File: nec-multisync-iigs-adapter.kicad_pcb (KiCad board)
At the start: 2 copper layers, 39.4 x 33 mm, 2 parts, among them J1 DA15_Plug

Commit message: V1 to Fab
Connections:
- J1 pad 1: GND -> /Red_GND
- J1 pad 13: GND -> /Blue_GND
- J1 pad 6: GND -> /Green_GND
- J2 pad 11: unconnected-(J2-Pad11) -> GND
- J2 pad 4: unconnected-(J2-Pad4) -> GND
- J2 pad 6: GND -> /Red_GND
- J2 pad 7: GND -> /Green_GND
- J2 pad 8: GND -> /Blue_GND
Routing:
- net /Blue_GND: track 0.00 -> 26.3 mm, vias 0 -> 2
- net /Green_GND: track 0.00 -> 24.0 mm, vias 0 -> 2
- net /Red_GND: track 0.00 -> 16.2 mm, vias 0 -> 1
- net /CSync: track 35.0 -> 29.4 mm, vias 2 -> 3
- net /Blue: track 29.0 -> 28.8 mm, vias 2 -> 3

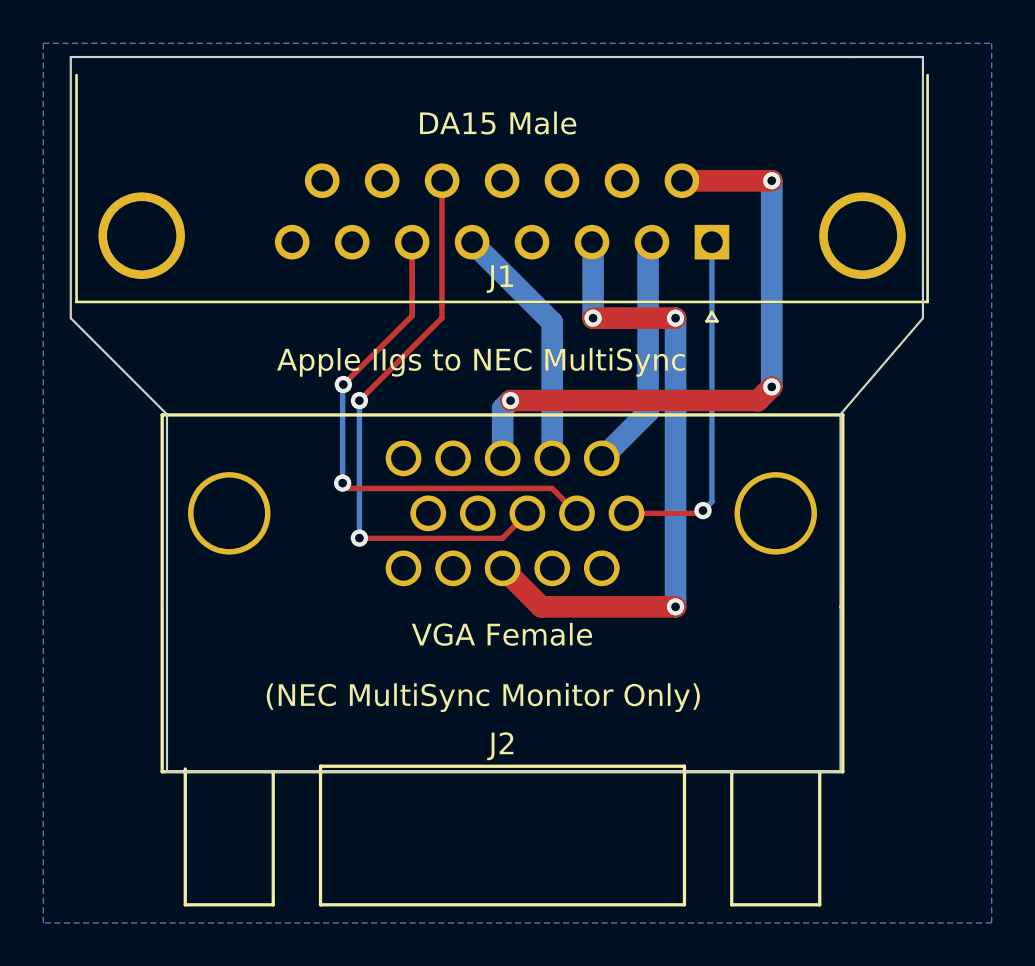
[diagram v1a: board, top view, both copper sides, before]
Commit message: Round-tracks plugin
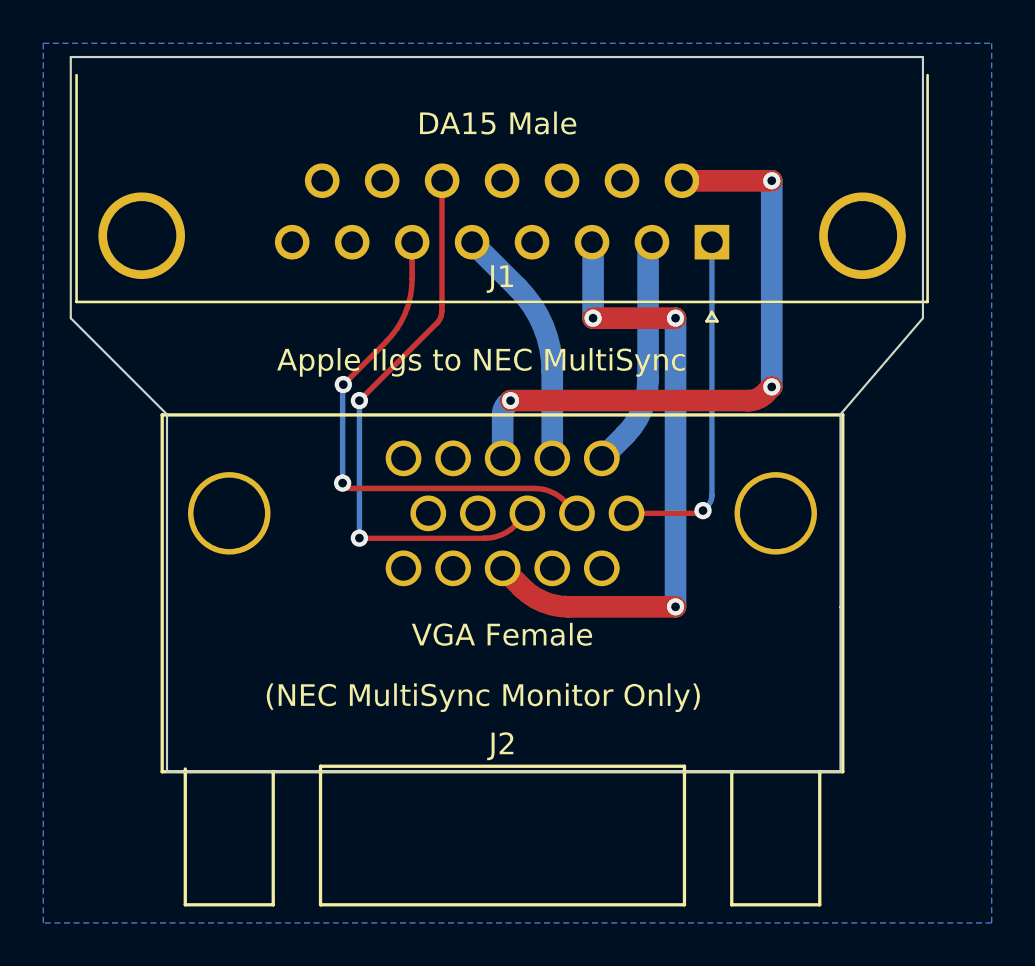
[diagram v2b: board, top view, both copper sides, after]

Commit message: Tie shields together; MultiSync now works
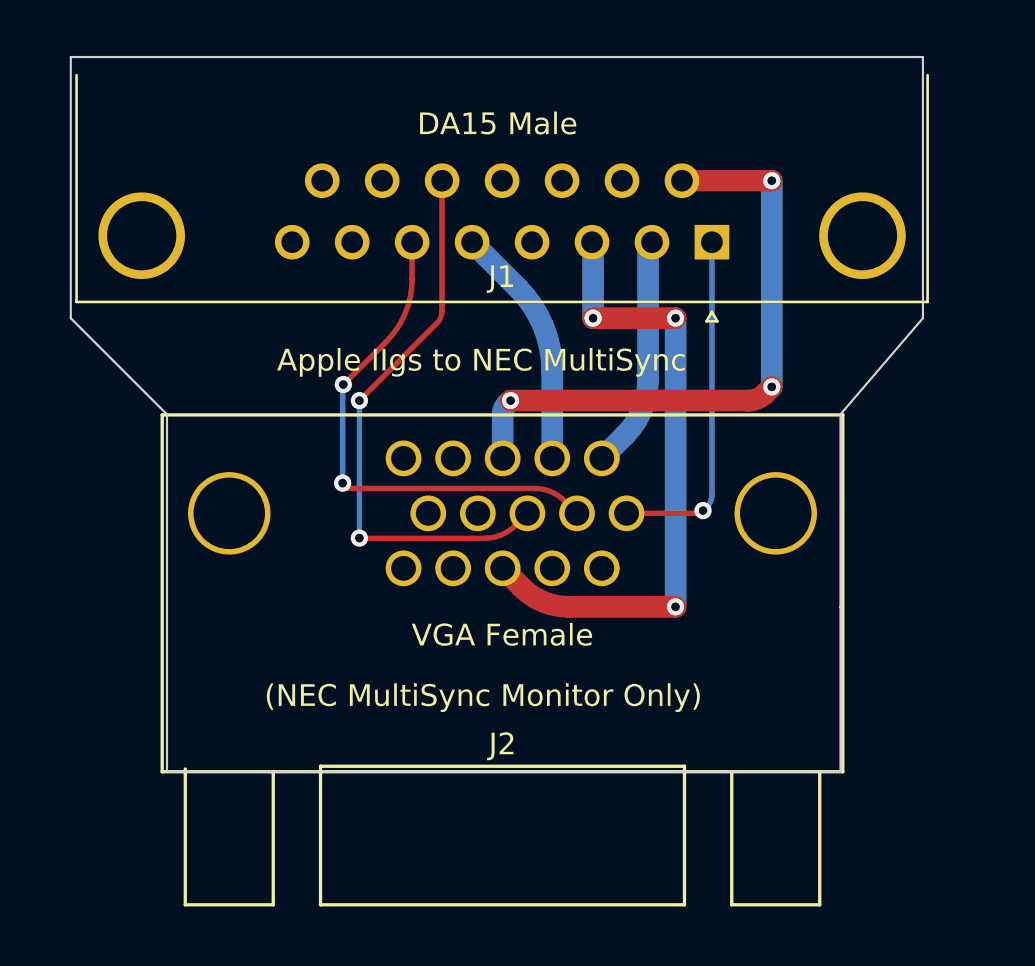
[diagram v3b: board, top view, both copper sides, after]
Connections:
- J2 pad 10: GND -> unconnected-(J2-Pad10)
- J2 pad 11: GND -> unconnected-(J2-Pad11)
- J2 pad 4: GND -> unconnected-(J2-Pad4)
- J2 pad 5: GND -> unconnected-(J2-Pad5)
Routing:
- removed copper zone on B.Cu, net GND
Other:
- board text added: "cs"
- board text added: "leadedsolder.com 2023-24 v0.3"
- board text removed: "leadedsolder.com 2023 v0.1"
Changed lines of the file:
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@@
       (drillshape 0)
       (scaleselection 1)
-      (outputdirectory "multisync-iigs-1")
+      (outputdirectory "multisync-iigs-2")
     )
   )
   (net 0 "")
-  (net 1 "GND")
+  (net 1 "unconnected-(J2-Pad4)")
   (net 2 "/Red")
   (net 3 "/CSync")
@@
   (net 19 "/Green_GND")
   (net 20 "/Blue_GND")
+  (net 21 "unconnected-(J2-Pad5)")
+  (net 22 "unconnected-(J2-Pad10)")
+  (net 23 "unconnected-(J2-Pad11)")
   (footprint "Connector_TE_AMP_HD15:FIXED-1-1734530-1" (layer "F.Cu")
     (at 115.196 91.948 180)
@@
       (net 8 "/Blue") (pintype "passive"))
     (pad "4" thru_hole circle (at 2.281936 14.351 180) (size 1.651 1.651) (drill 1.143) (layers "*.Cu" "*.Mask")
-      (net 1 "GND") (pintype "passive"))
+      (net 1 "unconnected-(J2-Pad4)") (pintype "passive+no_connect"))
     (pad "5" thru_hole circle (at 4.572 14.351 180) (size 1.651 1.651) (drill 1.143) (layers "*.Cu" "*.Mask")
-      (net 1 "GND") (pintype "passive"))
+      (net 21 "unconnected-(J2-Pad5)") (pintype "passive+no_connect"))
     (pad "6" thru_hole circle (at -5.730999 11.811 180) (size 1.651 1.651) (drill 1.143) (layers "*.Cu" "*.Mask")
       (net 17 "/Red_GND") (pintype "passive"))
@@
       (net 18 "unconnected-(J2-Pad9)") (pintype "passive+no_connect"))
     (pad "10" thru_hole circle (at 3.429 11.811 180) (size 1.651 1.651) (drill 1.143) (layers "*.Cu" "*.Mask")
-      (net 1 "GND") (pintype "passive"))
+      (net 22 "unconnected-(J2-Pad10)") (pintype "passive+no_connect"))
     (pad "11" thru_hole circle (at -4.587999 9.271 180) (size 1.651 1.651) (drill 1.143) (layers "*.Cu" "*.Mask")
-      (net 1 "GND") (pintype "passive"))
+      (net 23 "unconnected-(J2-Pad11)") (pintype "passive+no_connect"))
     (pad "12" thru_hole circle (at -2.297999 9.271 180) (size 1.651 1.651) (drill 1.143) (layers "*.Cu" "*.Mask")
       (net 16 "unconnected-(J2-Pad12)") (pintype "passive+no_connect"))
@@
     (effects (font (size 1 1) (thickness 0.15)) (justify left bottom mirror))
   )
-  (gr_text "leadedsolder.com 2023 v0.1" (at 125.73 73.66) (layer "B.SilkS")
+  (gr_text "leadedsolder.com 2023-24 v0.3" (at 127.635 73.66) (layer "B.SilkS")
     (effects (font (size 1 1) (thickness 0.15)) (justify left bottom mirror))
   )
   (gr_text "-5v" (at 109.982 70.104) (layer "B.SilkS")
+    (effects (font (size 1 1) (thickness 0.15)) (justify left bottom mirror))
+  )
+  (gr_text "cs" (at 120.2 69.9) (layer "B.SilkS")
     (effects (font (size 1 1) (thickness 0.15)) (justify left bottom mirror))
   )
@@
       )
     )
-  )
-  (zone (net 1) (net_name "GND") (layer "B.Cu") (hatch edge 0.5)
-    (connect_pads (clearance 0.5))
-    (min_thickness 0.25) (filled_areas_thickness no)
-    (fill yes (thermal_gap 0.5) (thermal_bridge_width 0.5))
-    (polygon
-      (pts
-        (xy 137.795 58.42)
-        (xy 137.795 99.06)
-        (xy 93.98 99.06)
-        (xy 93.98 58.42)
-      )
-    )

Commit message: Fix missing shield connection
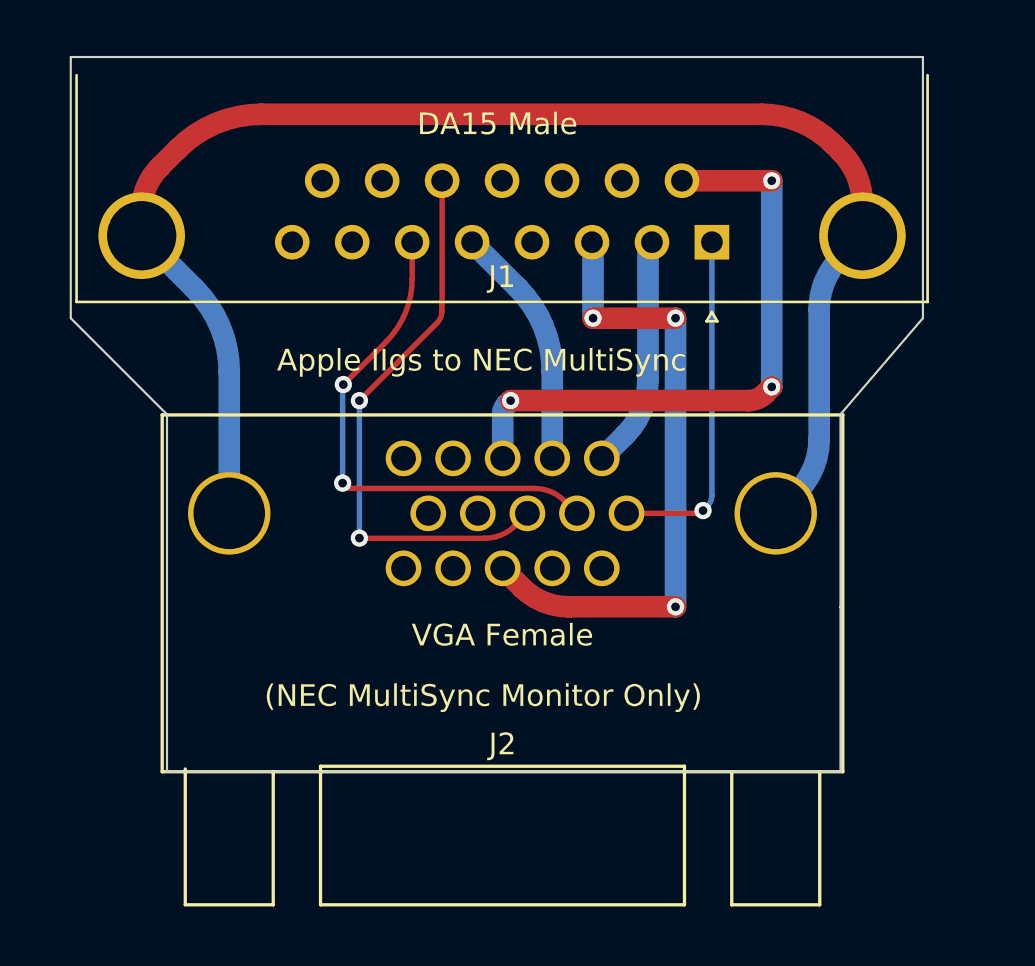
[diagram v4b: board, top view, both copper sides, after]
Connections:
- J1 pad 0: (no net) -> /Shield
- J2 pad 16: (no net) -> /Shield
- J2 pad 17: (no net) -> /Shield
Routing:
- net /Shield: track 0.00 -> 68.6 mm
